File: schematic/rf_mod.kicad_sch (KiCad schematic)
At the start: 3 parts, among them U23 4066

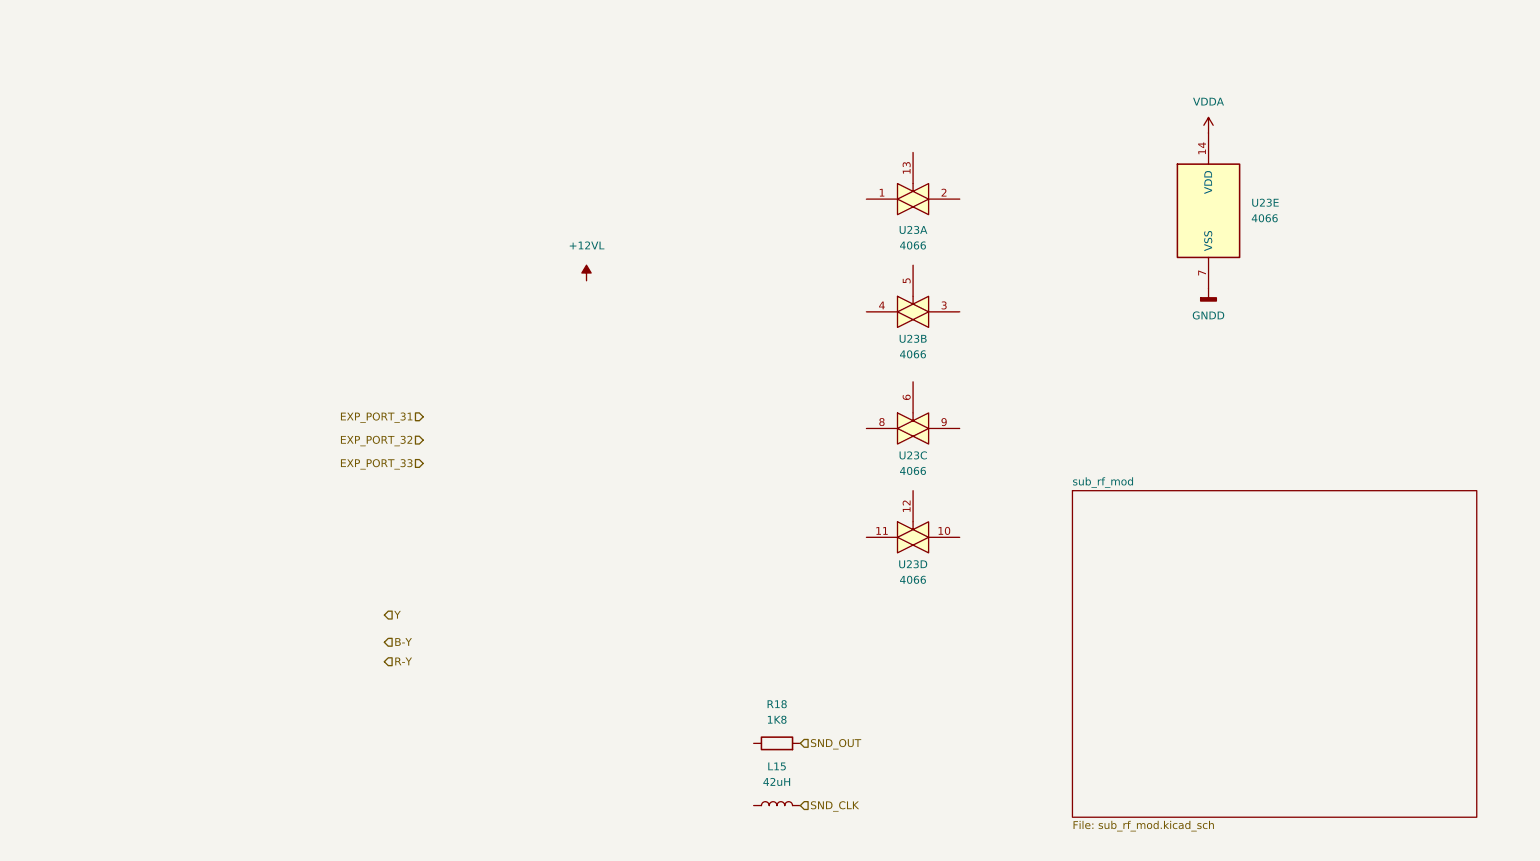
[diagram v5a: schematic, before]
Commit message: added rf mod section, this is very rough. Has mistakes for sure.
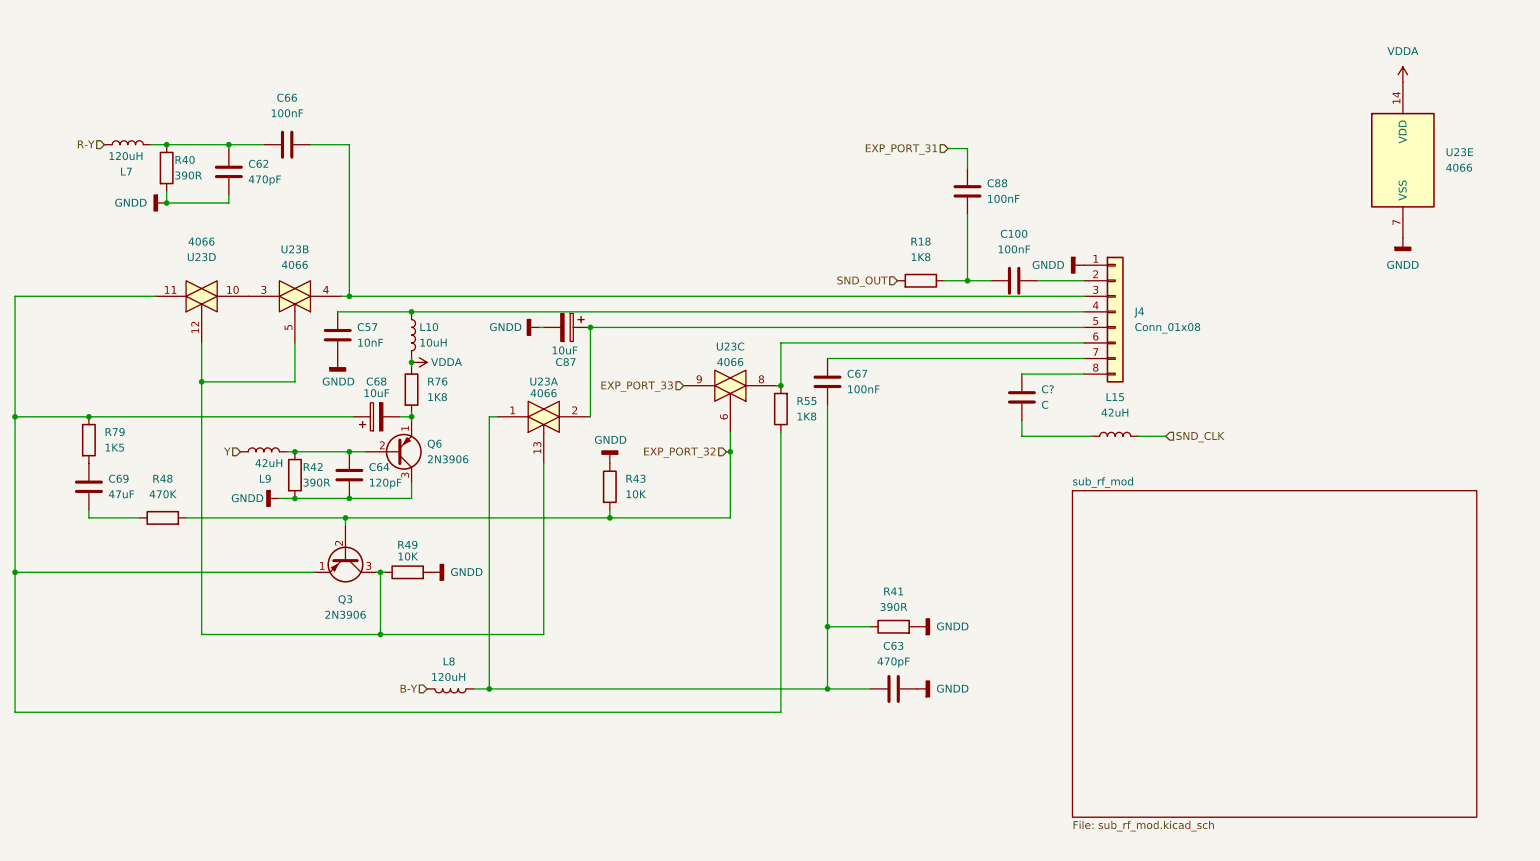
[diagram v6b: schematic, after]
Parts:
- added C100, C66, C67, C88: 100nF, symbol Device:C
- added C57: 10nF, symbol Device:C
- added C62, C63: 470pF, symbol Device:C
- added C64: 120pF, symbol Device:C
- added C68, C87: 10uF, symbol Device:C_Polarized
- added C69: 47uF, symbol Device:C
- added C?: C, symbol Device:C
- added J4: Conn_01x08, symbol Connector_Generic:Conn_01x08
- added L10: 10uH, symbol Device:L
- added L7, L8: 120uH, symbol Device:L
- added L9: 42uH, symbol Device:L
- added Q3, Q6: 2N3906, Package_TO_SOT_THT:TO-92_Inline, symbol Transistor_BJT:2N3906
- added R40, R41, R42: 390R, symbol Device:R
- added R43, R49: 10K, symbol Device:R
- added R48: 470K, symbol Device:R
- added R55, R76: 1K8, symbol Device:R
- added R79: 1K5, symbol Device:R
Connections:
- net B-Y: now also L8.2
- net EXP_PORT_31: now also C88.1
- net EXP_PORT_32: now also U23.6, Q3.2 (B), R43.2, R48.2
- net EXP_PORT_33: now also U23.9
- net GNDD: now also C57.2, C62.2, C63.2, C64.2, C87.2, J4.1 (Pin_1), Q6.3 (C), R40.2, R41.2, R42.2, R43.1, R49.2
- net R-Y: now also L7.2
- net VDDA: now also L10.2, R76.1
- net Y: now also L9.1
- net at L15.1: now also C?.2
- net at U23.8: now also J4.6 (Pin_6), R55.2
- net at U23.1: now also C63.1, C67.1, L8.1, R41.1
- net at U23.13: now also U23.12, U23.5, Q3.3 (C), R49.1
- net at U23.2: now also C87.1, J4.5 (Pin_5)
- net at U23.3: now also U23.10
- net at U23.4: now also C66.2, J4.3 (Pin_3)
- net at R18.1: now also C100.1, C88.2
- net at U23.11: now also C68.1, Q3.1 (E), R55.1, R79.1
- new net: C69.2, R48.1
- new net: C64.1, L9.2, Q6.2 (B), R42.1
- new net: C62.1, C66.1, L7.1, R40.1
- new net: C68.2, Q6.1 (E), R76.2
- new net: C?.1, J4.8 (Pin_8)
- new net: C57.1, J4.4 (Pin_4), L10.1
- new net: C67.2, J4.7 (Pin_7)
- new net: C69.1, R79.2
- new net: C100.2, J4.2 (Pin_2)
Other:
- moved on the sheet: L15, R18, U23A, U23B, U23C, U23D, U23E

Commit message: RF modulator completed, rough draft complete. Next step is to clean-up all pages.
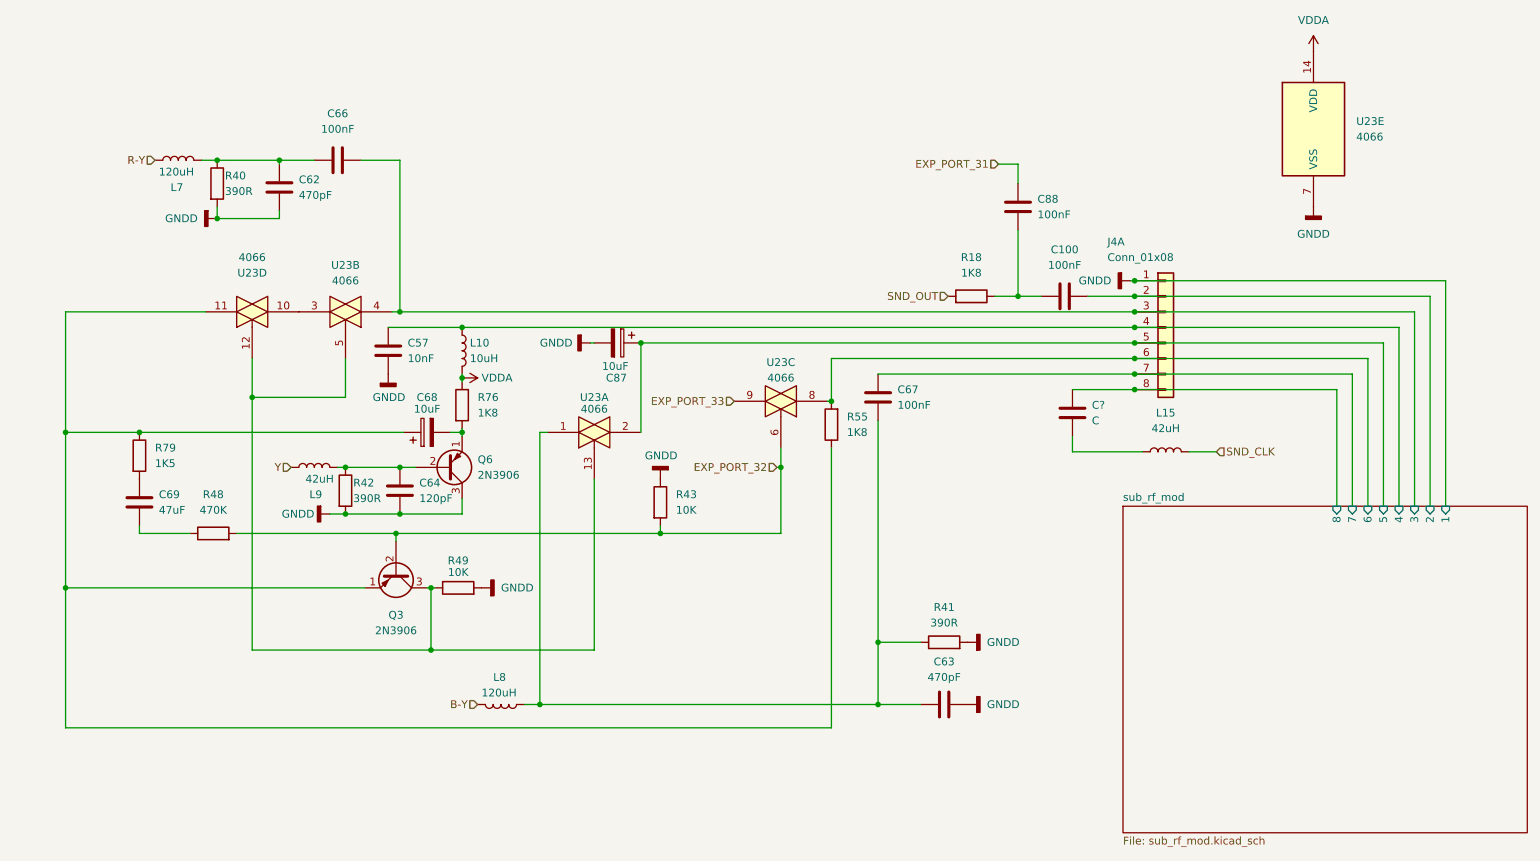
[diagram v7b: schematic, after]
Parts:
- renumbered J4 to J4A
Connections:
- net sub_rf_mod/3: now reaches C66.2, J4A.3 (Pin_3), U23.4
- net sub_rf_mod/6: now reaches J4A.6 (Pin_6), R55.2, U23.8
- net sub_rf_mod/8: now reaches C?.1, J4A.8 (Pin_8)
- net sub_rf_mod/5: now reaches C87.1, J4A.5 (Pin_5), U23.2
- net sub_rf_mod/4: now reaches C57.1, J4A.4 (Pin_4), L10.1
- net sub_rf_mod/7: now reaches C67.2, J4A.7 (Pin_7)
- net sub_rf_mod/2: now reaches C100.2, J4A.2 (Pin_2)
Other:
- sheet sub_rf_mod ports: added 1, 2, 3, 4, 5, 6, 7, 8; removed none
- moved on the sheet: C100, C57, C62, C63, C64, C66, C67, C68, C69, C87, C88, C?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

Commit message: cleaup of rf circuits. much better flow vs the original. Comparing to the wiki.console5.com/wiki/Colecovision shows many differences. Not sure I agree with it at all. Going to use the ADAM schematic instead since even the dual adjustable coils is not a thing in my circuit. Revision difference?
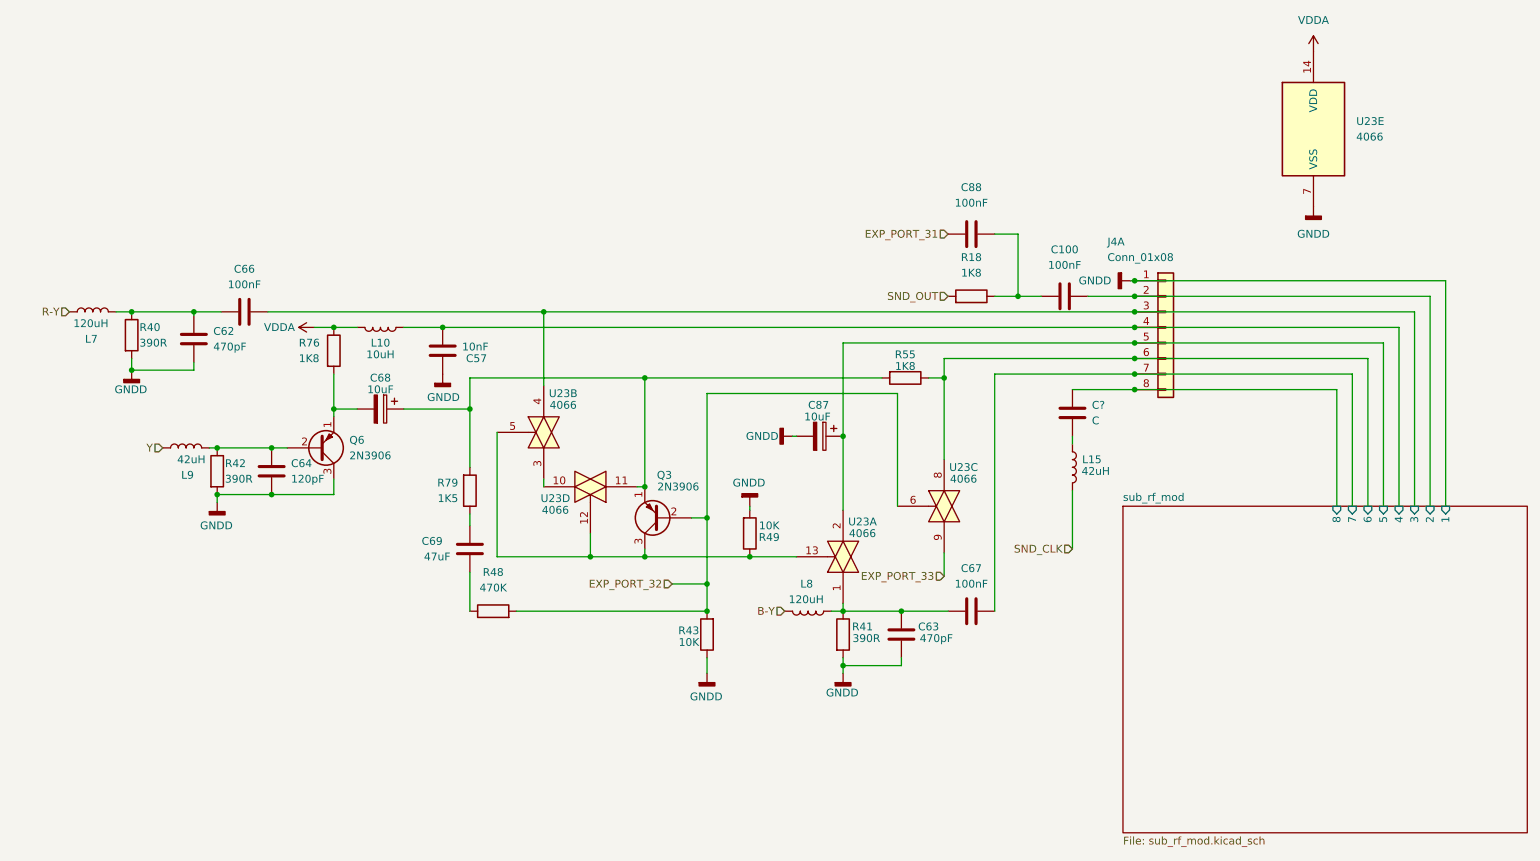
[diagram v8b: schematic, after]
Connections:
- net sub_rf_mod/3: now also C66.1; no longer C66.2
- net sub_rf_mod/6: now also R55.1; no longer R55.2
- net at R48.1: now also C69.1; no longer C69.2
- net at C62.1, L7.1, R40.1: now also C66.2; no longer C66.1
- net at C68.1, Q3.1 (E), U23.11: now also R55.2, R79.2; no longer R55.1, R79.1
- new net: C69.2, R79.1
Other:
- moved on the sheet: C57, C62, C63, C64, C66, C67, C68, C69, C87, C88, L10, L15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
